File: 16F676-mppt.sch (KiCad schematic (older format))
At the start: 50 parts, among them J1 S+, J2 S-, J3 VB+, J4 VB-, Q1 BUK9511-55A127, Q2 BUK9511-55A127, Q3 2N2222A, Q4 2N2222A, Q5 2N2907A, SW1 Write OP-AMP DIFF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

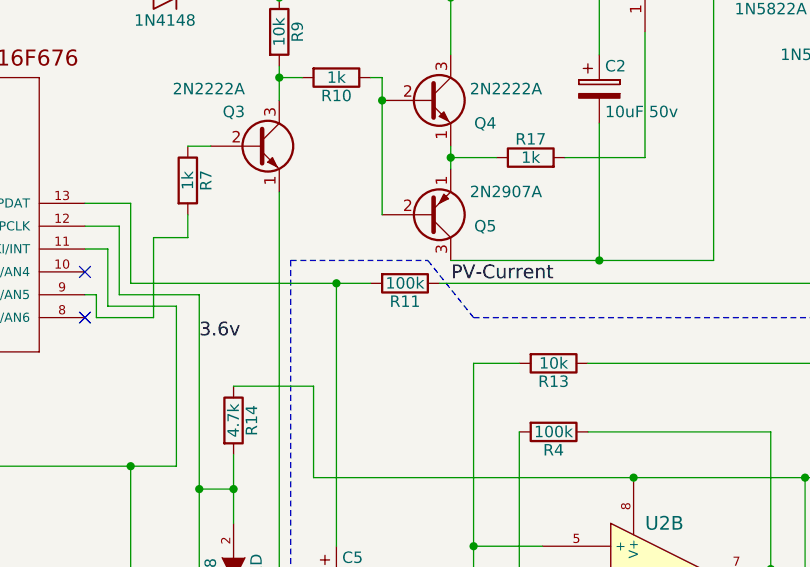
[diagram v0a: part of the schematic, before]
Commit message: R11 to 4.7k
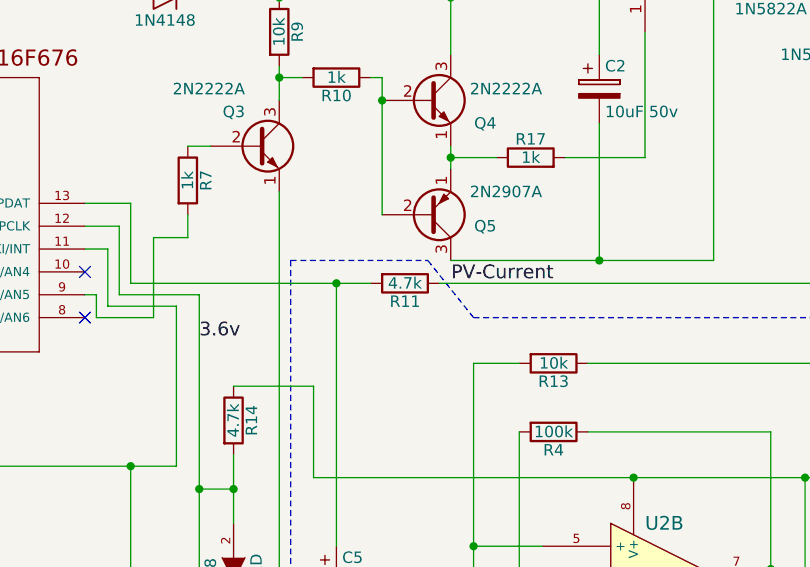
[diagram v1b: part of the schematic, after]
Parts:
- R11: value 100k -> 4.7k
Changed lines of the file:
@@
 Sheet 1 1
 Title "Simple MPPT with 16F676 v1"
-Date "2018-11-15"
-Rev "1.3"
+Date "2018-11-25"
+Rev "1.4"
 Comp ""
 Comment1 ""
@@
 P 6650 3600
 F 0 "R11" V 6730 3600 50  0000 C CNN
-F 1 "100k" V 6650 3600 50  0000 C CNN
+F 1 "4.7k" V 6650 3600 50  0000 C CNN
 F 2 "Resistors_THT:R_Axial_DIN0309_L9.0mm_D3.2mm_P12.70mm_Horizontal" V 6580 3600 30  0001 C CNN
 F 3 "" H 6650 3600 30  0000 C CNN

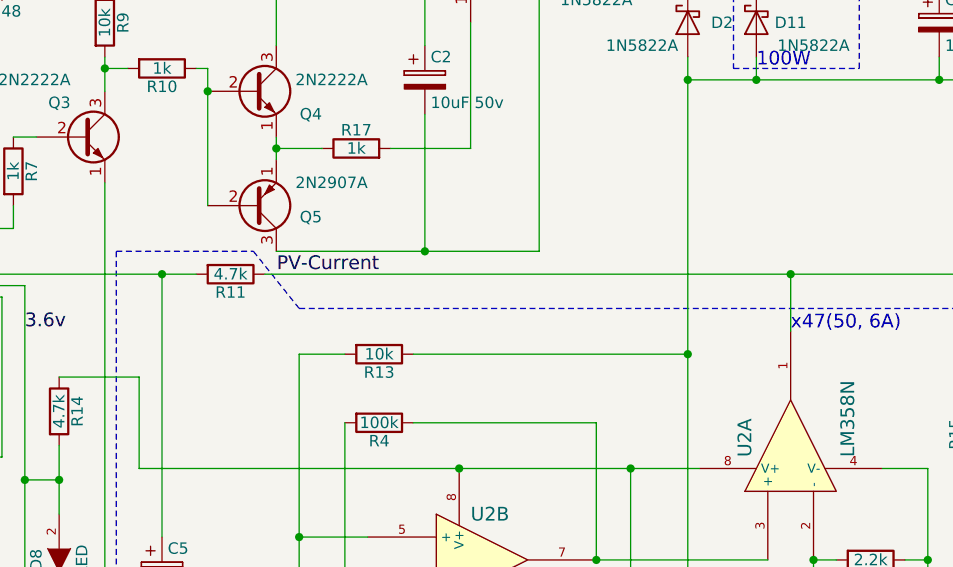
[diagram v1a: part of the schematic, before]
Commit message: Remove R11, it is a lot lower current sesing voltage.
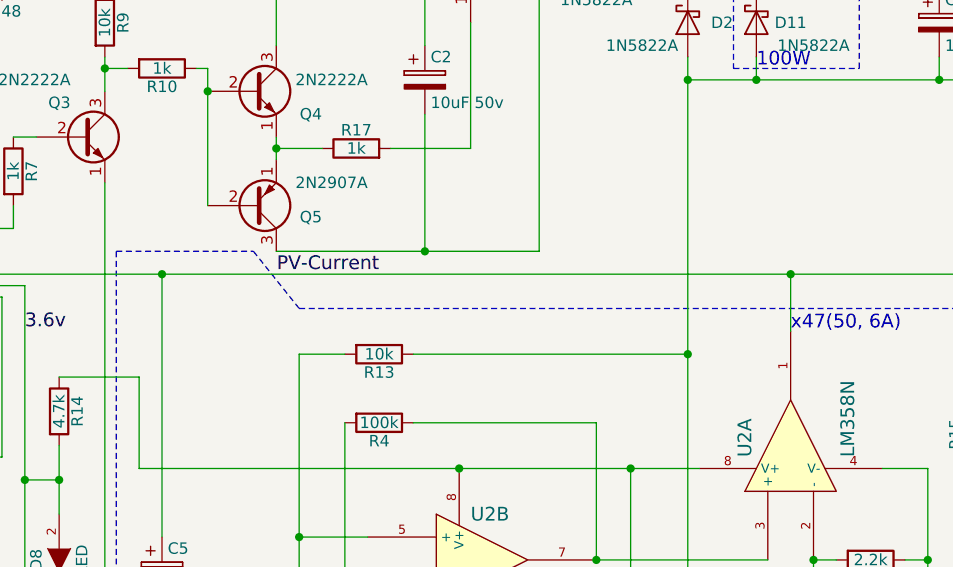
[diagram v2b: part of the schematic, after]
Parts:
- removed R11: 4.7k, Resistors_THT:R_Axial_DIN0309_L9.0mm_D3.2mm_P12.70mm_Horizontal, symbol Device:R
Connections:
- net PV-Current: now also C5.1, U3.13 (RA0/AN0/CIN+/ICSPDAT)
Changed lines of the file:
@@
 Sheet 1 1
 Title "Simple MPPT with 16F676 v1"
-Date "2018-11-25"
-Rev "1.4"
+Date "2018-11-29"
+Rev "1.5"
 Comp ""
 Comment1 ""
@@
 Heat Sink
 $Comp
-L Device:R R11
-U 1 1 55C4C21C
-P 6650 3600
-F 0 "R11" V 6730 3600 50  0000 C CNN
-F 1 "4.7k" V 6650 3600 50  0000 C CNN
-F 2 "Resistors_THT:R_Axial_DIN0309_L9.0mm_D3.2mm_P12.70mm_Horizontal" V 6580 3600 30  0001 C CNN
-F 3 "" H 6650 3600 30  0000 C CNN
-	1    6650 3600
-	0    1    1    0
-$EndComp
-$Comp
 L Device:R R12
 U 1 1 55C48C57
@@
 	9100 3850 9100 3600
 Wire Wire Line
-	6800 3600 9100 3600
-Wire Wire Line
 	9700 4450 9700 4850
 Connection ~ 8650 5600
@@
 	6350 5600 6100 5600
 Wire Wire Line
-	6350 3600 6500 3600
-Wire Wire Line
 	5450 5600 4100 5600
 Wire Wire Line
@@
 Wire Wire Line
 	7700 3050 7700 2500
+Wire Wire Line
+	6350 3600 9100 3600
 $EndSCHEMATC

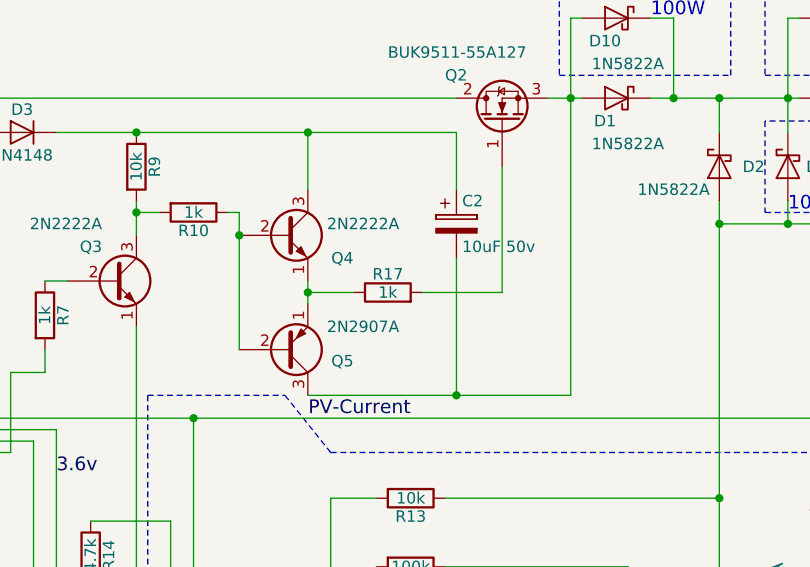
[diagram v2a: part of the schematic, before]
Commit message: Remove R17.
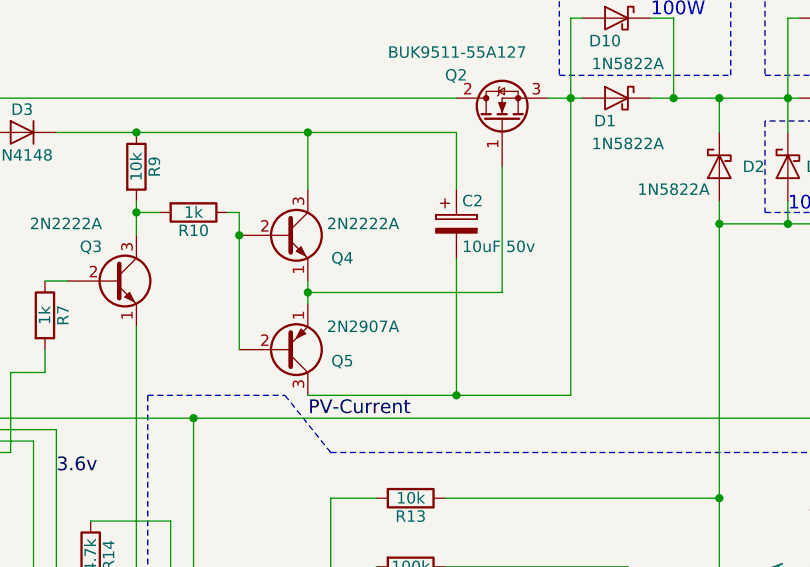
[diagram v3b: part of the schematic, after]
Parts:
- removed R17: 1k, Resistors_THT:R_Axial_DIN0309_L9.0mm_D3.2mm_P12.70mm_Horizontal, symbol Device:R
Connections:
- net at Q2.1 (G): now also Q4.1 (E), Q5.1 (E)
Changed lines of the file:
@@
 Wire Wire Line
 	8950 2200 9000 2200
-$Comp
-L Device:R R17
-U 1 1 5BF07E56
-P 7200 3050
-F 0 "R17" V 7280 3050 50  0000 C CNN
-F 1 "1k" V 7200 3050 50  0000 C CNN
-F 2 "Resistors_THT:R_Axial_DIN0309_L9.0mm_D3.2mm_P12.70mm_Horizontal" V 7130 3050 30  0001 C CNN
-F 3 "" H 7200 3050 30  0000 C CNN
-	1    7200 3050
-	0    -1   -1   0
-$EndComp
 Wire Wire Line
 	6850 3000 6850 3050
-Wire Wire Line
-	7050 3050 6850 3050
 Wire Wire Line
 	8000 2200 8000 3500
@@
 	6850 3050 6850 3100
 Wire Wire Line
-	7350 3050 7700 3050
-Wire Wire Line
 	7700 3050 7700 2500
 Wire Wire Line
 	6350 3600 9100 3600
+Wire Wire Line
+	6850 3050 7700 3050
 $EndSCHEMATC

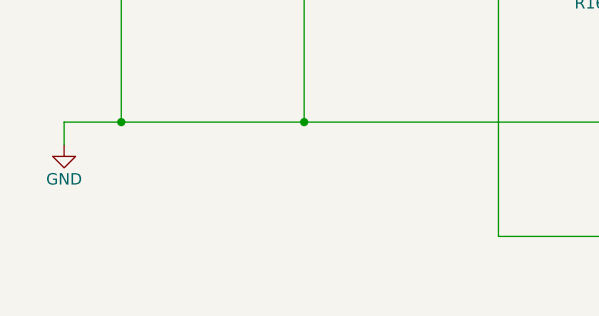
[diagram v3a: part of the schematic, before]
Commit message: C6 to optinal.
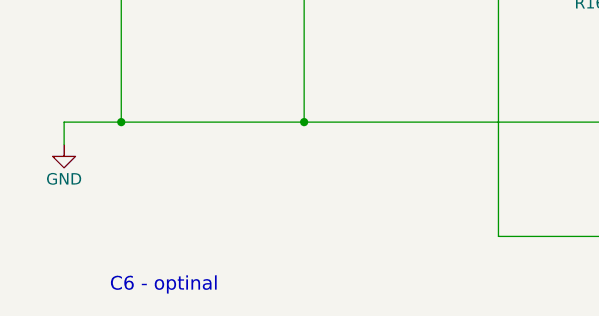
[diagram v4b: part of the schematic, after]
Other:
- note added: "C6 - optinal"
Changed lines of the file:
@@
 Wire Wire Line
 	6850 3050 7700 3050
+Text Notes 1450 6350 0    60   ~ 0
+C6 - optinal
 $EndSCHEMATC

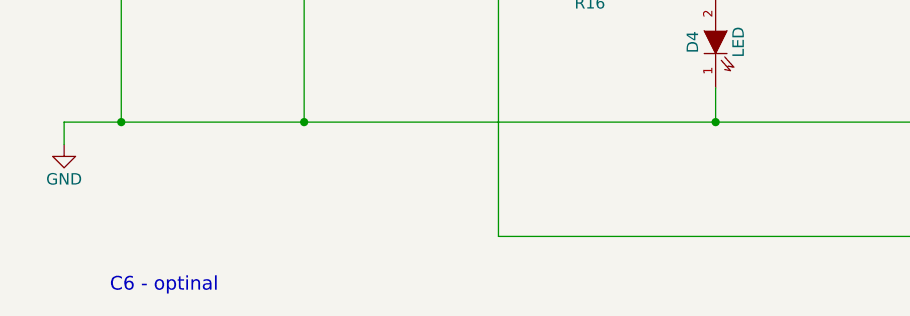
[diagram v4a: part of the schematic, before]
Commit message: Remove C6 for better power calculation. I assume low-pass filter but it make negative effect 'low voltage high current stuck'.
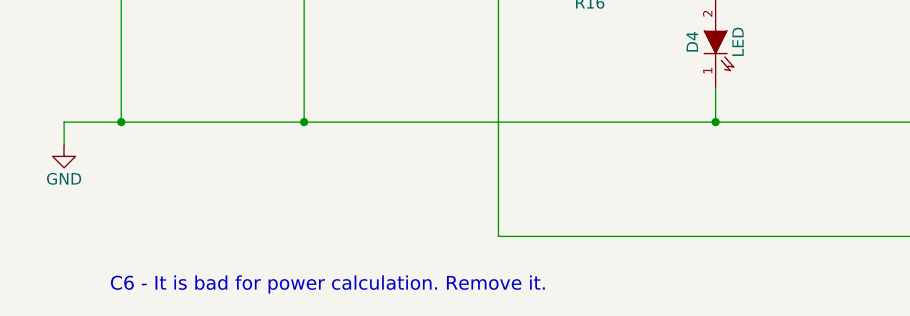
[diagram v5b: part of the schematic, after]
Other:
- note added: "C6 - It is bad for power calculation. Remove it."
- note removed: "C6 - optinal"
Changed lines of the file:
@@
 	6850 3050 7700 3050
 Text Notes 1450 6350 0    60   ~ 0
-C6 - optinal
+C6 - It is bad for power calculation. Remove it.
 $EndSCHEMATC

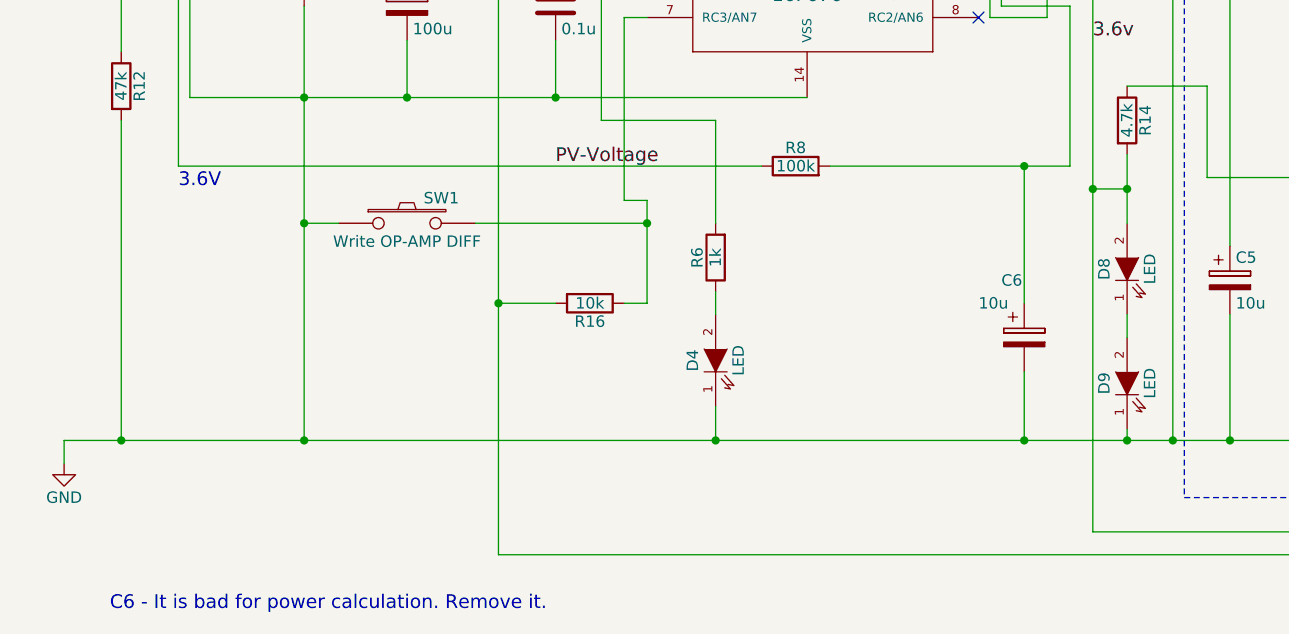
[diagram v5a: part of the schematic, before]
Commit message: Remove C6.
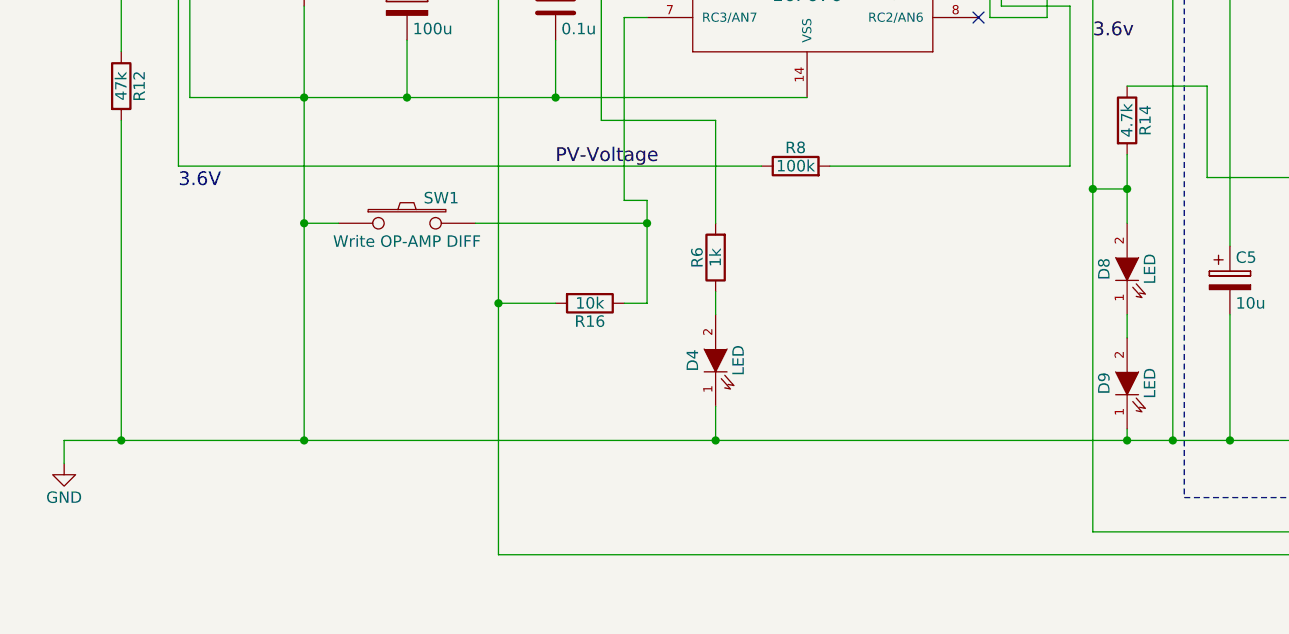
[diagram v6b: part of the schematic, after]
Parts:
- removed C6: 10u, Capacitors_THT:CP_Radial_D12.5mm_P5.00mm, symbol Device:CP
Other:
- note removed: "C6 - It is bad for power calculation. Remove it."
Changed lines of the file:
@@
 Sheet 1 1
 Title "Simple MPPT with 16F676 v1"
-Date "2018-11-29"
-Rev "1.5"
+Date "2018-12-17"
+Rev "1.6"
 Comp ""
 Comment1 ""
@@
 	1    0    0    -1
 $EndComp
-$Comp
-L Device:CP C6
-U 1 1 55D02AF9
-P 5450 5150
-F 0 "C6" H 5350 5400 50  0000 L CNN
-F 1 "10u" H 5250 5300 50  0000 L CNN
-F 2 "Capacitors_THT:CP_Radial_D12.5mm_P5.00mm" H 5488 5000 30  0001 C CNN
-F 3 "" H 5450 5150 60  0000 C CNN
-	1    5450 5150
-	1    0    0    -1
-$EndComp
 Text Label 8800 6000 0    60   ~ 0
 3.6v
@@
 	8400 6100 8400 4450
 Wire Wire Line
-	5450 5600 5450 5300
-Connection ~ 5450 5600
-Wire Wire Line
 	1750 3500 1750 4400
 Wire Wire Line
 	1750 4400 4300 4400
 Wire Wire Line
-	4600 4400 5450 4400
-Wire Wire Line
 	5650 4400 5650 3700
 Wire Wire Line
 	5650 3700 5350 3700
-Wire Wire Line
-	5450 5000 5450 4400
-Connection ~ 5450 4400
 Wire Wire Line
 	5900 4500 5750 4500
@@
 	8650 3950 8650 5200
 Wire Wire Line
-	5900 5600 5450 5600
-Wire Wire Line
 	6350 5600 6100 5600
-Wire Wire Line
-	5450 5600 4100 5600
-Wire Wire Line
-	5450 4400 5650 4400
 Wire Wire Line
 	5900 4500 5900 4650
@@
 Wire Wire Line
 	6850 3050 7700 3050
-Text Notes 1450 6350 0    60   ~ 0
-C6 - It is bad for power calculation. Remove it.
+Wire Wire Line
+	4600 4400 5650 4400
+Wire Wire Line
+	4100 5600 5900 5600
 $EndSCHEMATC

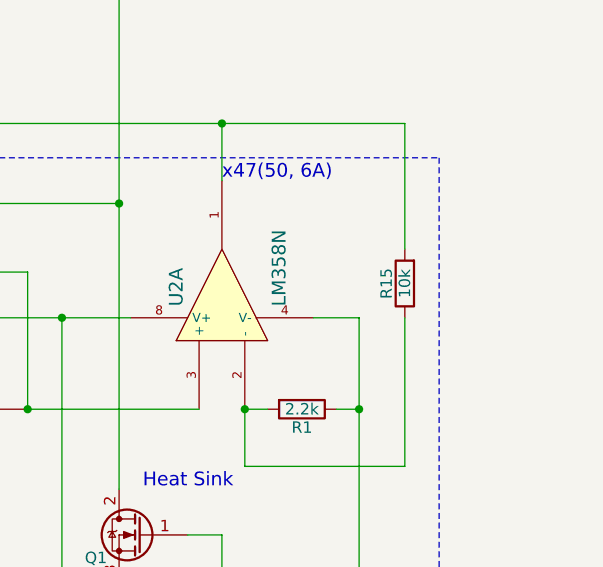
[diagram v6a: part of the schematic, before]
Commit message: R15 -> 4.7k. Current sensing is more higher than expected. 62mA -> 67mV.
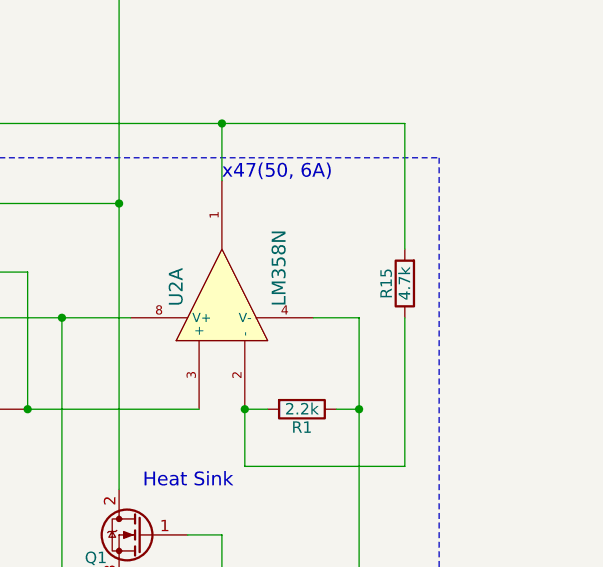
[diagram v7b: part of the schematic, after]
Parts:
- R15: value 10k -> 4.7k
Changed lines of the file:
@@
 P 9900 4300
 F 0 "R15" V 9980 4300 50  0000 C CNN
-F 1 "10k" V 9900 4300 50  0000 C CNN
+F 1 "4.7k" V 9900 4300 50  0000 C CNN
 F 2 "Resistors_THT:R_Axial_DIN0309_L9.0mm_D3.2mm_P12.70mm_Horizontal" V 9830 4300 50  0001 C CNN
 F 3 "" H 9900 4300 50  0000 C CNN

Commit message: update R15 value.
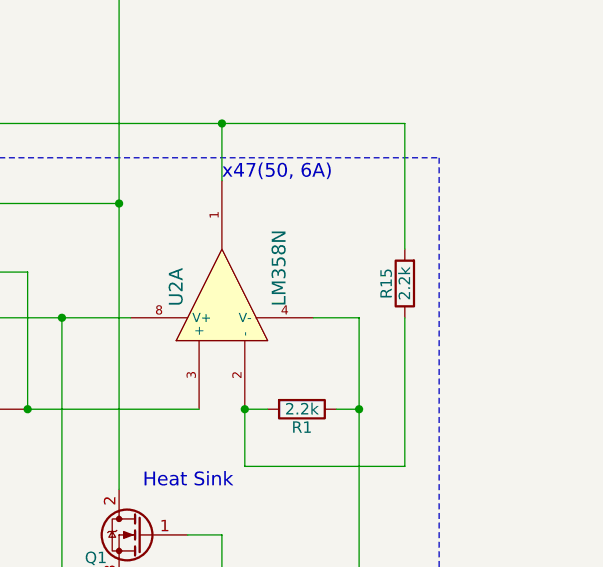
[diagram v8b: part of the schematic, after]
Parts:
- R15: value 4.7k -> 2.2k
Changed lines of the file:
@@
 P 9900 4300
 F 0 "R15" V 9980 4300 50  0000 C CNN
-F 1 "4.7k" V 9900 4300 50  0000 C CNN
+F 1 "2.2k" V 9900 4300 50  0000 C CNN
 F 2 "Resistors_THT:R_Axial_DIN0309_L9.0mm_D3.2mm_P12.70mm_Horizontal" V 9830 4300 50  0001 C CNN
 F 3 "" H 9900 4300 50  0000 C CNN
